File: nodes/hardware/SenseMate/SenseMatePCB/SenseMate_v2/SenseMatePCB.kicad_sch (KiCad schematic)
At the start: 15 parts, among them J1 Conn_01x04, J2 Conn_02x06_Counter_Clockwise 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, M1 Motor_DC, Q1 2SC1815, Q2 2SC1815, SW5 SW_DPDT_x2, U1 XIAO-nRF52840-Plus-SMD, U2 RFM95W-868S2

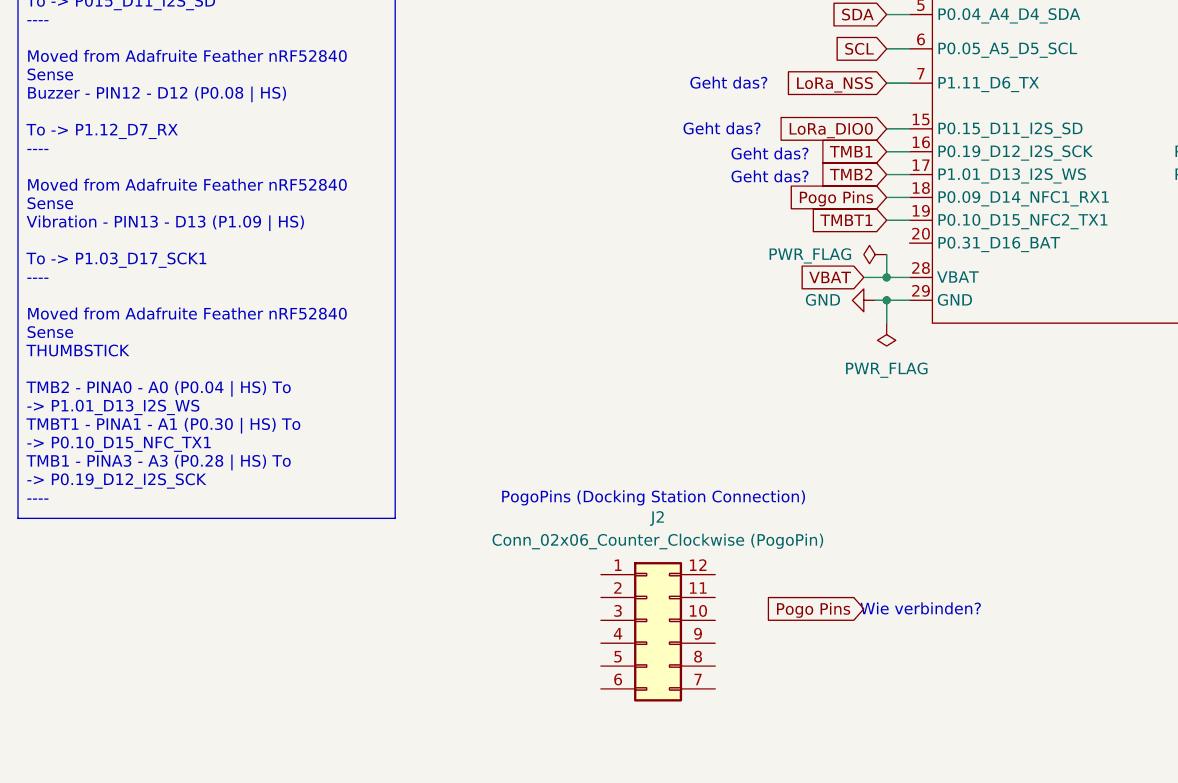
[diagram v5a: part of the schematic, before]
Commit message: reorganized design of board
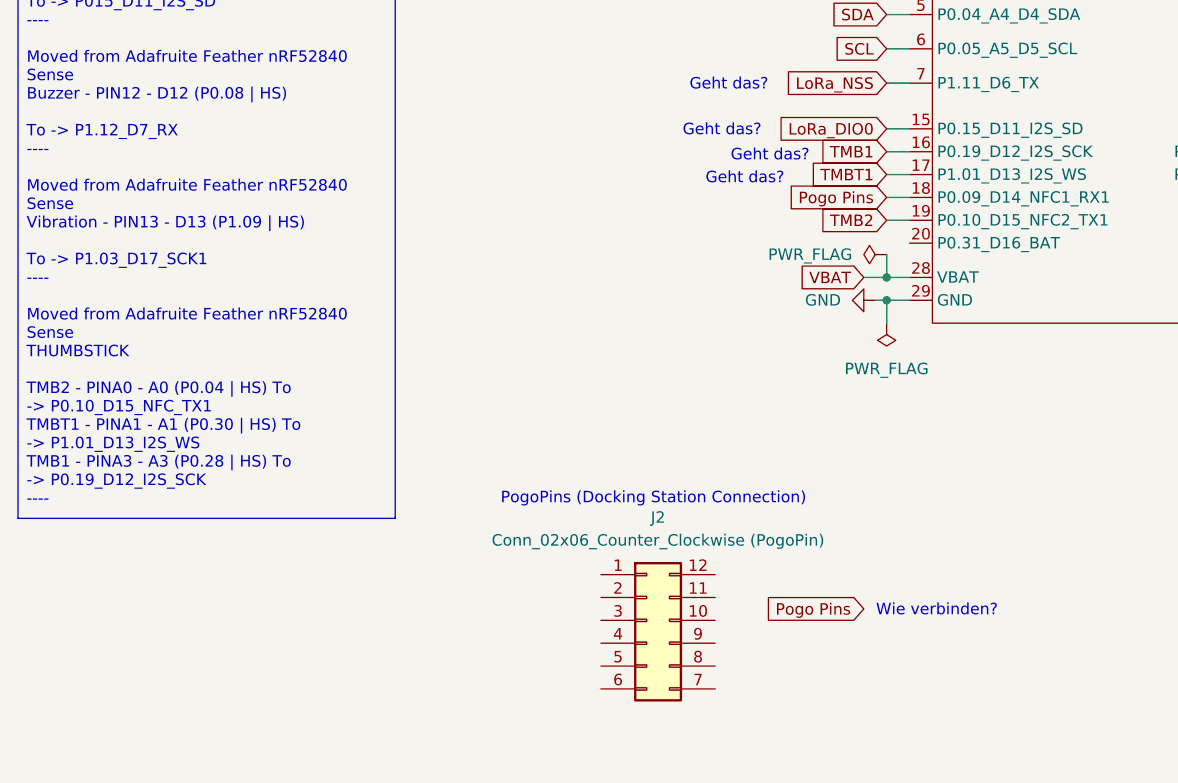
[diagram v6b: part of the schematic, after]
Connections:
- net TMB2: now also U1.19 (P0.10_D15_NFC2_TX1); no longer U1.17 (P1.01_D13_I2S_WS)
- net TMBT1: now also U1.17 (P1.01_D13_I2S_WS); no longer U1.19 (P0.10_D15_NFC2_TX1)

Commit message: pcb version 2.1 done
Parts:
- added J3: Conn_Coaxial, Connector_Coaxial:U.FL_Molex_MCRF_73412-0110_Vertical, symbol Connector:Conn_Coaxial
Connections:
- net LoRa_NSS: now also U1.21 (P1.03_D17_SCK1); no longer U1.7 (P1.11_D6_TX)
- net VIB_EN: now also U1.7 (P1.11_D6_TX); no longer U1.21 (P1.03_D17_SCK1)
- net at U2.9 (ANT): now also J3.2 (Ext)

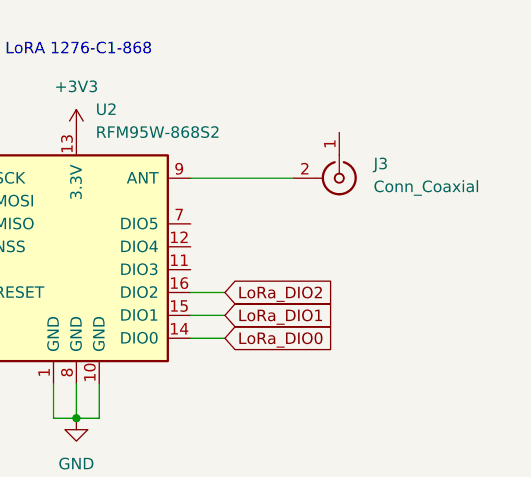
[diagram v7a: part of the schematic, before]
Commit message: nodes/hardware/PCB: save some space with different arrangement
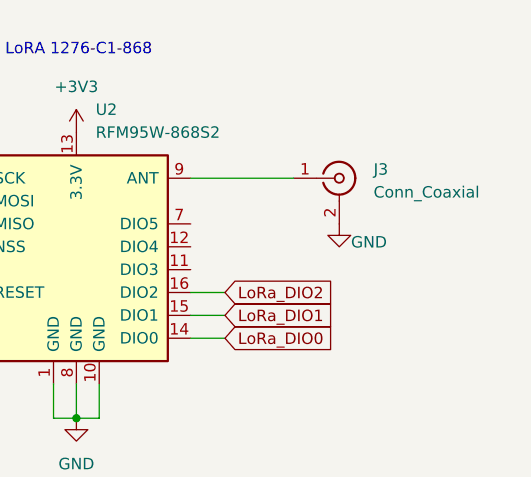
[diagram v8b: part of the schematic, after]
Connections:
- net GND: now also J3.2 (Ext)
- net at J3.1 (In): now also U2.9 (ANT)
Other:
- moved on the sheet: J3
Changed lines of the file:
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@@
+	)
+	(symbol
+		(lib_id "power:GND")
+		(at 196.85 34.29 0)
+		(unit 1)
+		(body_style 1)
+		(exclude_from_sim no)
+		(in_bom yes)
+		(on_board yes)
+		(in_pos_files yes)
+		(dnp no)
+		(property "Reference" "#PWR018"
+			(at 196.85 40.64 0)
+			(hide yes)
+			(show_name no)
+			(do_not_autoplace no)
+			(effects
+				(font
+					(size 1.27 1.27)
+				)
+			)
+		)
+		(property "Value" "GND"
+			(at 200.152 36.322 0)
+			(show_name no)
+			(do_not_autoplace no)
+			(effects
+				(font
+					(size 1.27 1.27)
+				)
+			)
+		)
+		(property "Footprint" ""
+			(at 196.85 34.29 0)
+			(hide yes)
+			(show_name no)
+			(do_not_autoplace no)
+			(effects
+				(font
+					(size 1.27 1.27)
+				)
+			)
+		)
+		(property "Datasheet" ""
+			(at 196.85 34.29 0)
+			(hide yes)
+			(show_name no)
+			(do_not_autoplace no)
+			(effects
+				(font
+					(size 1.27 1.27)
+				)
+			)
+		)
+		(property "Description" "Power symbol creates a global label with name \"GND\" , ground"
+			(at 196.85 34.29 0)
+			(hide yes)
+			(show_name no)
+			(do_not_autoplace no)
+			(effects
+				(font
+					(size 1.27 1.27)
+				)
+			)
+		)
+		(pin "1"
+		)
+		(instances
+			(project "SenseMatePCB"
+				(path "/70e40189-008f-4f72-8f4c-fe289f3548a4"
+					(reference "#PWR018")
+					(unit 1)
+				)
+			)
+		)
 	)
 	(symbol
@@
 	(symbol
 		(lib_id "Connector:Conn_Coaxial")
-		(at 196.85 29.21 270)
+		(at 196.85 29.21 0)
 		(unit 1)
 		(body_style 1)
@@
 		(fields_autoplaced yes)
 		(property "Reference" "J3"
-			(at 200.66 27.6224 90)
+			(at 200.66 28.2331 0)
 			(show_name no)
 			(do_not_autoplace no)
@@
 		)
 		(property "Value" "Conn_Coaxial"
-			(at 200.66 30.1624 90)
-			(show_name no)
-			(do_not_autoplace no)
+			(at 200.66 30.7731 0)
+			(show_name no)
+			(do_not_autoplace no)
